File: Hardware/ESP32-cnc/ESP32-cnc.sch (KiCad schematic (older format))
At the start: 85 parts, among them J1 Inputs, J10 Y-Servo, J11 X_STEP_B, J12 Y_STEP_B, J13 Spindle On/Off, J14 X_STEP_A, J15 Y_STEP_A, J16 Z_STEP, J2 12-18V DC, J3 Conn_01x19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

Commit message: minor updates
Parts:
- J8: value Enable Spindle -> PWM Spindle (5V)
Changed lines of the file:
@@
 P 6400 8300
 F 0 "J8" H 6480 8292 50  0000 L CNN
-F 1 "Enable Spindle" H 6480 8201 50  0000 L CNN
+F 1 "PWM Spindle (5V)" H 6480 8201 50  0000 L CNN
 F 2 "Pin_Headers:Pin_Header_Straight_1x04_Pitch2.54mm" H 6400 8300 50  0001 C CNN
 F 3 "~" H 6400 8300 50  0001 C CNN

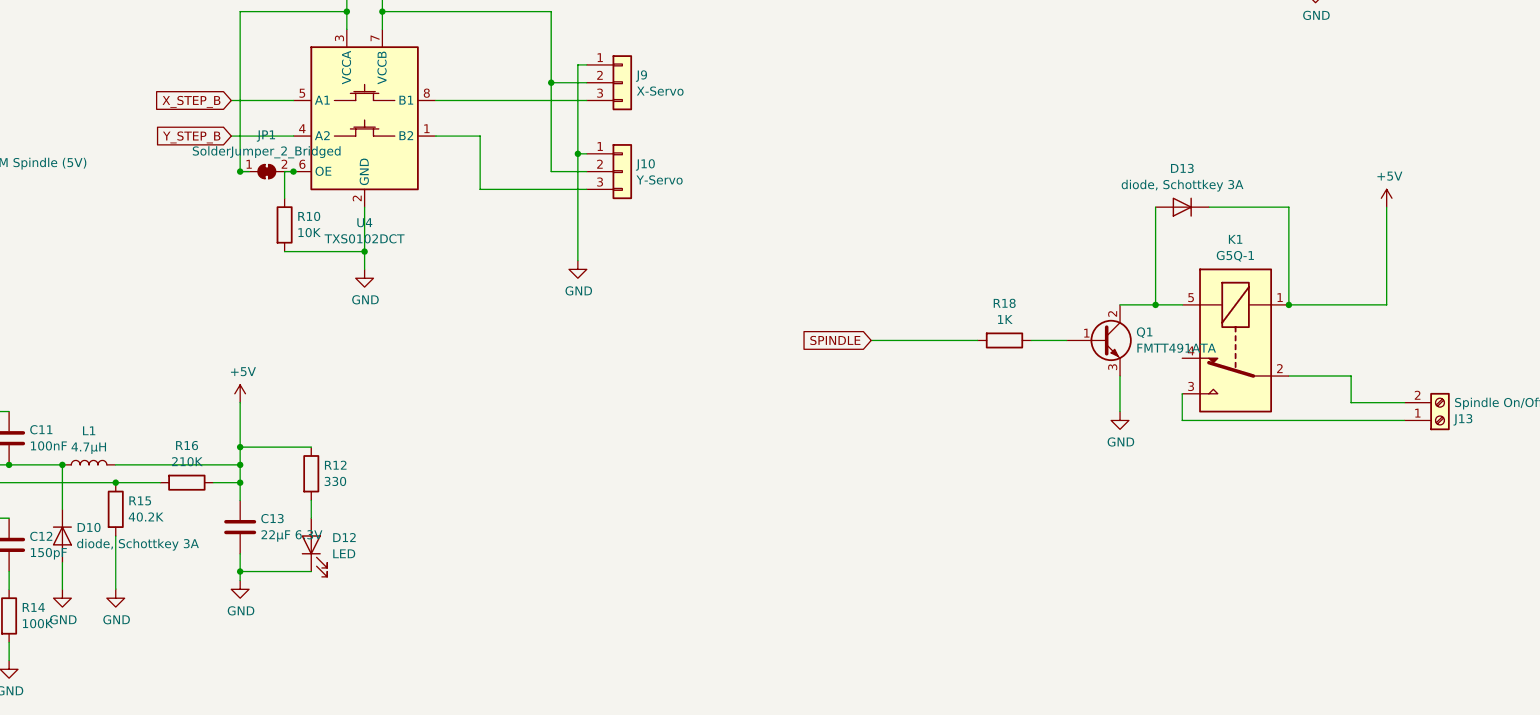
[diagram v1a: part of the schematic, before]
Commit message: footprint adaption
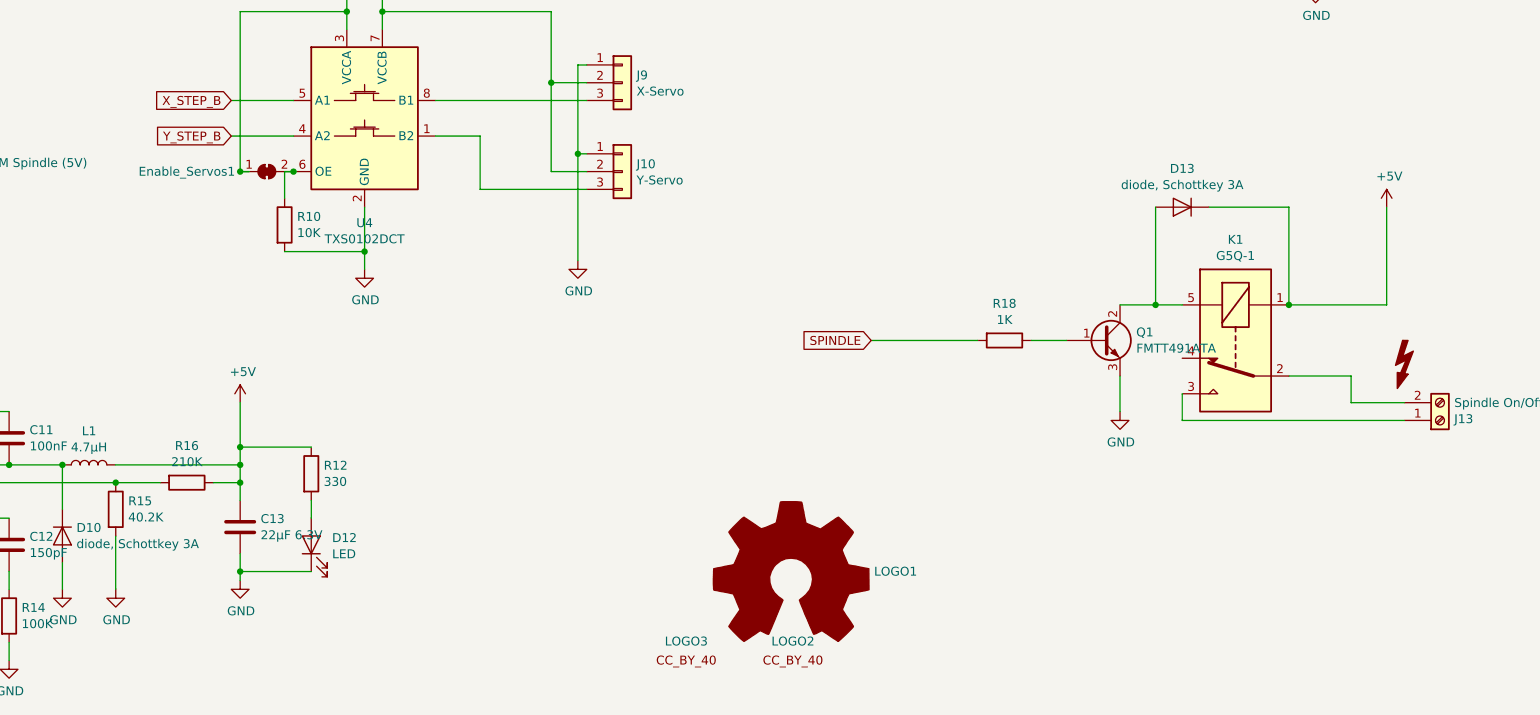
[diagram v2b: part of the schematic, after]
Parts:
- added LOGO1: Logo_Open_Hardware_Large, Symbols:OSHW-Symbol_22.3x20mm_SilkScreen, symbol Graphic:Logo_Open_Hardware_Large
- added LOGO2: SYM_CC_BY, Symbols:Symbol_CreativeCommonsPublicDomain_SilkScreenTop_Small, symbol MyGraphic:SYM_CC_BY
- added LOGO3: SYM_CC_BY, Symbols:Symbol_CC-Attribution_CopperTop_Small, symbol MyGraphic:SYM_CC_BY
- added SYM1: SYM_Flash_Small, Symbols:Symbol_HighVoltage_Type2_CopperTop_VerySmall, symbol Graphic:SYM_Flash_Small
- Enable_Servos1: renamed from JP1; value SolderJumper_2_Bridged -> Enable_Servos
- X_MS1: value X2_MS1 -> X_MS1
- X_MS2: value X2_MS2 -> X_MS2
- X_MS3: value X2_MS3 -> X_MS3
- Y2_MS1: value X2_MS1 -> Y2_MS1
- Y2_MS2: value X2_MS2 -> Y2_MS2
- Y2_MS3: value X2_MS3 -> Y2_MS3
- Y_MS1: value X2_MS1 -> Y_MS1
- Y_MS2: value X2_MS2 -> Y_MS2
- Y_MS3: value X2_MS3 -> Y_MS3
- Z_MS1: value X2_MS1 -> Z_MS1
- Z_MS2: value X2_MS2 -> Z_MS2
- Z_MS3: value X2_MS3 -> Z_MS3
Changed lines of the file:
@@
 Wire Wire Line
 	7350 5600 8050 5600
-$Comp
-L Jumper:SolderJumper_2_Bridged JP1
-U 1 1 5E2E7A8F
-P 8100 8250
-F 0 "JP1" H 8100 8455 50  0000 C CNN
-F 1 "SolderJumper_2_Bridged" H 8100 8364 50  0000 C CNN
-F 2 "Jumpers:SolderJumper-2_P1.3mm_Bridged_RoundedPad1.0x1.5mm" H 8100 8250 50  0001 C CNN
-F 3 "~" H 8100 8250 50  0001 C CNN
-	1    8100 8250
-	1    0    0    -1
-$EndComp
-Wire Wire Line
-	8000 8250 7950 8250
-Wire Wire Line
-	7950 8250 7950 7350
-Connection ~ 7950 8250
 Connection ~ 8550 7350
 Wire Wire Line
@@
 Wire Wire Line
 	7950 7350 8550 7350
-Connection ~ 8250 8250
 Wire Wire Line
 	9000 850  9000 2000
@@
 P 12800 6600
 F 0 "Z_MS1" H 12400 6600 50  0000 C CNN
-F 1 "X2_MS1" H 12800 6714 50  0001 C CNN
+F 1 "Z_MS1" H 12800 6714 50  0001 C CNN
 F 2 "Jumpers:SolderJumper-2_P1.3mm_Bridged_RoundedPad1.0x1.5mm" H 12800 6600 50  0001 C CNN
 F 3 "~" H 12800 6600 50  0001 C CNN
@@
 P 12800 6700
 F 0 "Z_MS2" H 12400 6700 50  0000 C CNN
-F 1 "X2_MS2" H 12800 6814 50  0001 C CNN
+F 1 "Z_MS2" H 12800 6814 50  0001 C CNN
 F 2 "Jumpers:SolderJumper-2_P1.3mm_Bridged_RoundedPad1.0x1.5mm" H 12800 6700 50  0001 C CNN
 F 3 "~" H 12800 6700 50  0001 C CNN
@@
 P 12800 6800
 F 0 "Z_MS3" H 12400 6800 50  0000 C CNN
-F 1 "X2_MS3" H 12800 6914 50  0001 C CNN
+F 1 "Z_MS3" H 12800 6914 50  0001 C CNN
 F 2 "Jumpers:SolderJumper-2_P1.3mm_Bridged_RoundedPad1.0x1.5mm" H 12800 6800 50  0001 C CNN
 F 3 "~" H 12800 6800 50  0001 C CNN
@@
 P 9150 4250
 F 0 "Y2_MS1" H 8750 4250 50  0000 C CNN
-F 1 "X2_MS1" H 9150 4364 50  0001 C CNN
+F 1 "Y2_MS1" H 9150 4364 50  0001 C CNN
 F 2 "Jumpers:SolderJumper-2_P1.3mm_Bridged_RoundedPad1.0x1.5mm" H 9150 4250 50  0001 C CNN
 F 3 "~" H 9150 4250 50  0001 C CNN
@@
 P 9150 4350
 F 0 "Y2_MS2" H 8750 4350 50  0000 C CNN
-F 1 "X2_MS2" H 9150 4464 50  0001 C CNN
+F 1 "Y2_MS2" H 9150 4464 50  0001 C CNN
 F 2 "Jumpers:SolderJumper-2_P1.3mm_Bridged_RoundedPad1.0x1.5mm" H 9150 4350 50  0001 C CNN
 F 3 "~" H 9150 4350 50  0001 C CNN
@@
 P 9150 4450
 F 0 "Y2_MS3" H 8750 4450 50  0000 C CNN
-F 1 "X2_MS3" H 9150 4564 50  0001 C CNN
+F 1 "Y2_MS3" H 9150 4564 50  0001 C CNN
 F 2 "Jumpers:SolderJumper-2_P1.3mm_Bridged_RoundedPad1.0x1.5mm" H 9150 4450 50  0001 C CNN
 F 3 "~" H 9150 4450 50  0001 C CNN
@@
 P 12800 4350
 F 0 "Y_MS1" H 12400 4350 50  0000 C CNN
-F 1 "X2_MS1" H 12800 4464 50  0001 C CNN
+F 1 "Y_MS1" H 12800 4464 50  0001 C CNN
 F 2 "Jumpers:SolderJumper-2_P1.3mm_Bridged_RoundedPad1.0x1.5mm" H 12800 4350 50  0001 C CNN
 F 3 "~" H 12800 4350 50  0001 C CNN
@@
 P 12800 4450
 F 0 "Y_MS2" H 12400 4450 50  0000 C CNN
-F 1 "X2_MS2" H 12800 4564 50  0001 C CNN
+F 1 "Y_MS2" H 12800 4564 50  0001 C CNN
 F 2 "Jumpers:SolderJumper-2_P1.3mm_Bridged_RoundedPad1.0x1.5mm" H 12800 4450 50  0001 C CNN
 F 3 "~" H 12800 4450 50  0001 C CNN
@@
 P 12800 4550
 F 0 "Y_MS3" H 12400 4550 50  0000 C CNN
-F 1 "X2_MS3" H 12800 4664 50  0001 C CNN
+F 1 "Y_MS3" H 12800 4664 50  0001 C CNN
 F 2 "Jumpers:SolderJumper-2_P1.3mm_Bridged_RoundedPad1.0x1.5mm" H 12800 4550 50  0001 C CNN
 F 3 "~" H 12800 4550 50  0001 C CNN
@@
 P 12750 2000
 F 0 "X_MS1" H 12350 2000 50  0000 C CNN
-F 1 "X2_MS1" H 12750 2114 50  0001 C CNN
+F 1 "X_MS1" H 12750 2114 50  0001 C CNN
 F 2 "Jumpers:SolderJumper-2_P1.3mm_Bridged_RoundedPad1.0x1.5mm" H 12750 2000 50  0001 C CNN
 F 3 "~" H 12750 2000 50  0001 C CNN
@@
 P 12750 2100
 F 0 "X_MS2" H 12350 2100 50  0000 C CNN
-F 1 "X2_MS2" H 12750 2214 50  0001 C CNN
+F 1 "X_MS2" H 12750 2214 50  0001 C CNN
 F 2 "Jumpers:SolderJumper-2_P1.3mm_Bridged_RoundedPad1.0x1.5mm" H 12750 2100 50  0001 C CNN
 F 3 "~" H 12750 2100 50  0001 C CNN
@@
 P 12750 2200
 F 0 "X_MS3" H 12350 2200 50  0000 C CNN
-F 1 "X2_MS3" H 12750 2314 50  0001 C CNN
+F 1 "X_MS3" H 12750 2314 50  0001 C CNN
 F 2 "Jumpers:SolderJumper-2_P1.3mm_Bridged_RoundedPad1.0x1.5mm" H 12750 2200 50  0001 C CNN
 F 3 "~" H 12750 2200 50  0001 C CNN
@@
 Connection ~ 12600 850
 Connection ~ 12650 5450
+Connection ~ 8250 8250
+Connection ~ 7950 8250
+Wire Wire Line
+	7950 8250 7950 7350
+Wire Wire Line
+	8000 8250 7950 8250
+$Comp
+L Jumper:SolderJumper_2_Bridged Enable_Servos1
+U 1 1 5E2E7A8F
+P 8100 8250
+F 0 "Enable_Servos1" H 7650 8250 50  0000 C CNN
+F 1 "Enable_Servos" H 7900 8150 50  0001 C CNN
+F 2 "Jumpers:SolderJumper-2_P1.3mm_Bridged_RoundedPad1.0x1.5mm" H 8100 8250 50  0001 C CNN
+F 3 "~" H 8100 8250 50  0001 C CNN
+	1    8100 8250
+	1    0    0    -1
+$EndComp
+$Comp
+L Graphic:Logo_Open_Hardware_Large LOGO1
+U 1 1 5E370774
+P 11050 10550
+F 0 "LOGO1" H 11516 10600 50  0000 L CNN
+F 1 "Logo_Open_Hardware_Large" H 11050 10150 50  0001 C CNN
+F 2 "Symbols:OSHW-Symbol_22.3x20mm_SilkScreen" H 11050 11067 50  0001 C CNN
+F 3 "~" H 11050 10550 50  0001 C CNN
+	1    11050 10550
+	1    0    0    -1
+$EndComp
+$Comp
+L Graphic:SYM_Flash_Small SYM1
+U 1 1 5E371D74
+P 14500 9350
+F 0 "SYM1" V 14410 9350 50  0001 C CNN
+F 1 "SYM_Flash_Small" V 14590 9350 50  0001 C CNN
+F 2 "Symbols:Symbol_HighVoltage_Type2_CopperTop_VerySmall" H 14500 9325 50  0001 C CNN
+F 3 "~" H 14900 9250 50  0001 C CNN
+	1    14500 9350
+	1    0    0    -1
+$EndComp
+$Comp
+L MyGraphic:SYM_CC_BY LOGO2
+U 1 1 5E3C9D0D
+P 11050 11000
+F 0 "LOGO2" H 11060 11107 50  0000 C CNN
+F 1 "SYM_CC_BY" H 11060 11107 50  0001 C CNN
+F 2 "Symbols:Symbol_CreativeCommonsPublicDomain_SilkScreenTop_Small" H 11050 11000 50  0001 C CNN
+F 3 "" H 11050 11000 50  0001 C CNN
+	1    11050 11000
+	1    0    0    -1
+$EndComp
+$Comp
+L MyGraphic:SYM_CC_BY LOGO3
+U 1 1 5E3FA9CE
+P 10450 11000
+F 0 "LOGO3" H 10460 11107 50  0000 C CNN
+F 1 "SYM_CC_BY" H 10460 11107 50  0001 C CNN
+F 2 "Symbols:Symbol_CC-Attribution_CopperTop_Small" H 10450 11000 50  0001 C CNN
+F 3 "" H 10450 11000 50  0001 C CNN
+	1    10450 11000
+	1    0    0    -1
+$EndComp
 $EndSCHEMATC
